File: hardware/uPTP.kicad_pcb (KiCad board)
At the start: 4 copper layers, 40 x 50 mm, 78 parts, among them J1 PPS_UFL, J2 PPS_SMA, J3 LED, J4 UART_HDR, J5 HC-RJ45-055-7, J6 AUX_PWR, J7 PROG, U1 XC6206P332MR-G, U2 SI3404-A-GMR, U3 CH32V307WCU6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

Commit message: Route one
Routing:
- net /Ethernet and POE/ETH_D_ISO_RX_P: track 6.89 -> 9.89 mm
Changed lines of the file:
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@@
+	)
+	(segment
+		(start 160.53 111.13)
+		(end 159.7 110.3)
+		(width 0.3)
+		(layer "F.Cu")
+		(net 14)
 	)
 	(segment
 		(start 160.53 113.4425)
-		(end 160.53 112)
+		(end 160.53 111.13)
 		(width 0.3)
 		(layer "F.Cu")
@@
 	)
 	(segment
-		(start 160.53 112)
-		(end 159.275 110.745)
+		(start 159.7 110.3)
+		(end 159.7 106.7)
 		(width 0.3)
 		(layer "F.Cu")
@@
 	)
 	(segment
-		(start 159.275 110.745)
-		(end 159.275 106.275)
+		(start 159.7 106.7)
+		(end 158.885 105.885)
 		(width 0.3)
 		(layer "F.Cu")
@@
 	)
 	(segment
-		(start 159.275 106.275)
-		(end 158.885 105.885)
-		(width 0.3)
-		(layer "F.Cu")
-		(net 14)
+		(start 157.942794 109.73087)
+		(end 158.636258 110.424334)
+		(width 0.3)
+		(layer "F.Cu")
+		(net 15)
 	)
 	(segment
 		(start 157.47 113.4425)
-		(end 157.47 112)
-		(width 0.3)
-		(layer "F.Cu")
-		(net 15)
-	)
-	(segment
-		(start 158.425 108.425)
+		(end 157.47 111.93)
+		(width 0.3)
+		(layer "F.Cu")
+		(net 15)
+	)
+	(segment
+		(start 158.97567 110.424333)
+		(end 159.060522 110.339479)
+		(width 0.3)
+		(layer "F.Cu")
+		(net 15)
+	)
+	(segment
+		(start 158.725 108.425)
 		(end 157.2 108.425)
 		(width 0.3)
@@
 	)
 	(segment
-		(start 157.47 112)
-		(end 158.725 110.745)
-		(width 0.3)
-		(layer "F.Cu")
-		(net 15)
-	)
-	(segment
-		(start 158.725 110.745)
-		(end 158.725 108.725)
-		(width 0.3)
-		(layer "F.Cu")
-		(net 15)
-	)
-	(segment
-		(start 158.725 108.725)
-		(end 158.425 108.425)
+		(start 159.060522 110.339479)
+		(end 159.15 110.25)
+		(width 0.3)
+		(layer "F.Cu")
+		(net 15)
+	)
+	(segment
+		(start 159.15 108.85)
+		(end 158.725 108.425)
+		(width 0.3)
+		(layer "F.Cu")
+		(net 15)
+	)
+	(segment
+		(start 159.15 110.25)
+		(end 159.15 108.85)
+		(width 0.3)
+		(layer "F.Cu")
+		(net 15)
+	)
+	(segment
+		(start 158.211993 110.848596)
+		(end 157.51853 110.155133)
+		(width 0.3)
+		(layer "F.Cu")
+		(net 15)
+	)
+	(segment
+		(start 157.47 111.93)
+		(end 158.211992 111.188008)
+		(width 0.3)
+		(layer "F.Cu")
+		(net 15)
+	)
+	(segment
+		(start 157.518529 109.815723)
+		(end 157.603384 109.730869)
+		(width 0.3)
+		(layer "F.Cu")
+		(net 15)
+	)
+	(arc
+		(start 157.603384 109.730869)
+		(mid 157.773089 109.660575)
+		(end 157.942794 109.73087)
+		(width 0.3)
+		(layer "F.Cu")
+		(net 15)
+	)
+	(arc
+		(start 158.211992 111.188008)
+		(mid 158.282287 111.018302)
+		(end 158.211993 110.848596)
+		(width 0.3)
+		(layer "F.Cu")
+		(net 15)
+	)
+	(arc
+		(start 158.636258 110.424334)
+		(mid 158.805963 110.494629)
+		(end 158.97567 110.424333)
+		(width 0.3)
+		(layer "F.Cu")
+		(net 15)
+	)
+	(arc
+		(start 157.51853 110.155133)
+		(mid 157.448236 109.985427)
+		(end 157.518529 109.815723)
 		(width 0.3)
 		(layer "F.Cu")
@@
 		)
 	)
+	(generated
+		(type tuning_pattern)
+		(name "Tuning Pattern")
+		(layer "F.Cu")
+		(base_line
+			(pts
+				(xy 158.211992 111.188008) (xy 159.15 110.25) (xy 159.15 108.85) (xy 158.725 108.425) (xy 157.2 108.425)
+			)
+		)
+		(base_line_coupled
+			(pts
+				(xy 159.7 110.3) (xy 159.7 108.425)
+			)
+		)
+		(corner_radius_percent 80)
+		(end
+			(xy 157.2 108.425)
+		)
+		(initial_side "left")
+		(last_diff_pair_gap 0.18)
+		(last_netname "/Ethernet and POE/ETH_D_ISO_RX_P")
+		(last_status "too_short")
+		(last_track_width 0.3)
+		(last_tuning "-0.0000 mm (too short)")
+		(max_amplitude 1.5)
+		(min_amplitude 0.2)
+		(min_spacing 0.6)
+		(origin
+			(xy 158.211992 111.188008)
+		)
+		(override_custom_rules no)
+		(rounded yes)
+		(single_sided no)
+		(target_length 1000000)
+		(target_length_max 1000000)
+		(target_length_min 0)
+		(target_skew 0)
+		(target_skew_max 2147.483647)
+		(target_skew_min 0)
+		(tuning_mode "diff_pair_skew")
+		(members "0bae2fc2-0211-45f2-b836-eb4cafed9c5f" "277517a9-859e-45f5-9af7-aa420a2b5a6d"
+			"5b8daaf6-95e9-43ba-83e5-7fa846d3aed7" "5c5d8d0c-bf78-4b6e-a43a-62fd2599fa16"
+			"5cfc8858-2205-4a4b-a7d7-186fc4d642b2" "72fc6440-39a9-4567-8914-2f6c557ffe45"
+			"79a215ad-b56f-4a34-89d0-93d5ca94d08a" "8e7def69-ecf8-4a06-9879-d4727dc86b5c"
+			"95469f03-8aef-4034-a113-e60f53eb121f" "d9926ceb-a356-417e-8caa-e14e1cfa22e8"
+			"e493b56a-8677-492b-b57a-b9f674e9be6f" "fd0d77c2-6f58-4c50-8de8-89af1b98e4d6"
+		)
+	)

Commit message: All length match
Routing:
- net /Ethernet and POE/ETH_D_ISO_TX_P: track 13.2 -> 21.8 mm
- net /Ethernet and POE/ETH_D_TX_P: track 12.1 -> 13.2 mm
- net /Ethernet and POE/ETH_D_ISO_TX_N: track 21.3 -> 21.9 mm

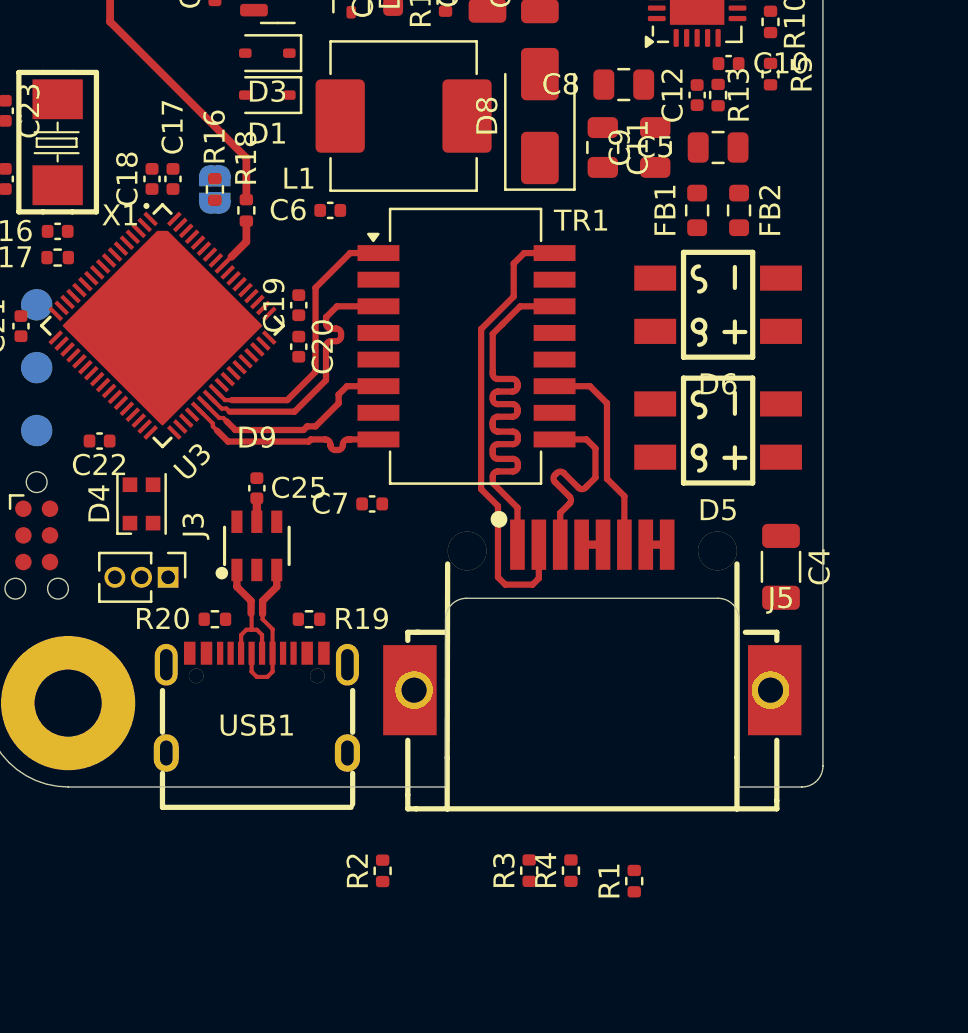
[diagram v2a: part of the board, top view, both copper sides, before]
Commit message: ISO ETH Section Done
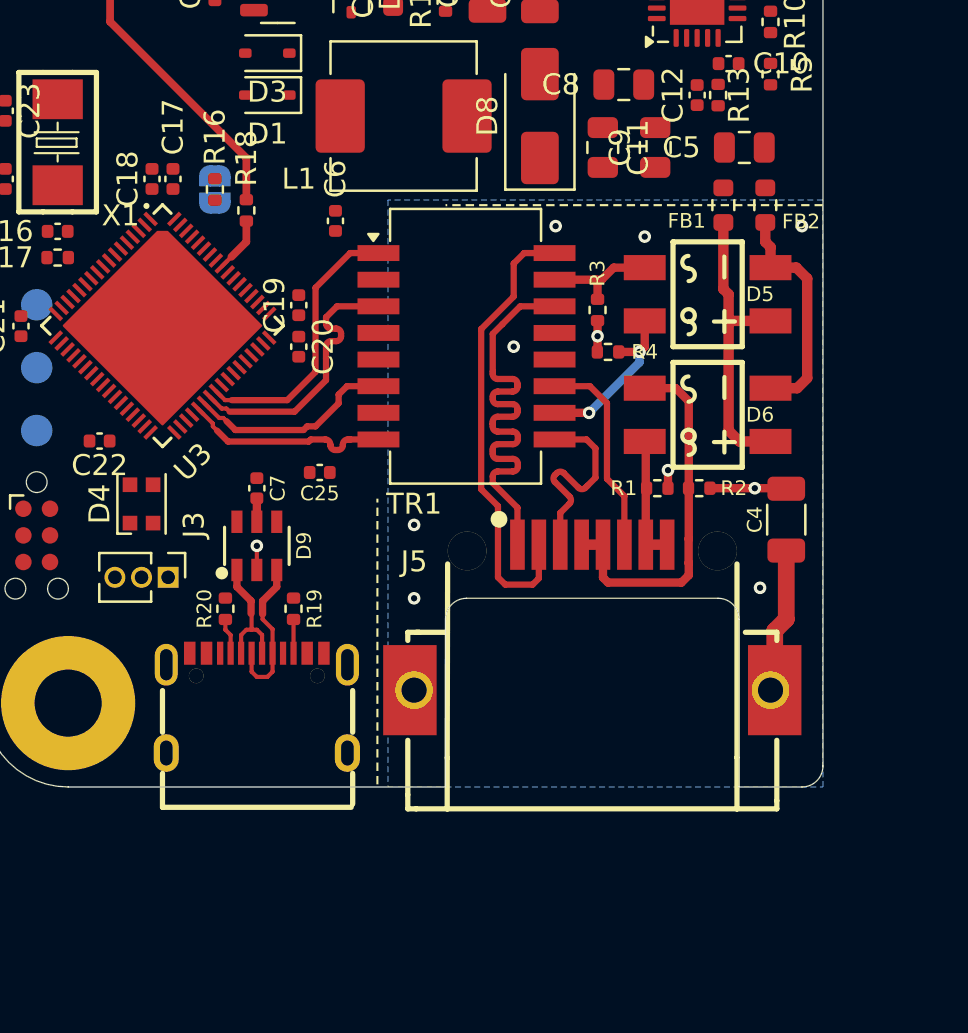
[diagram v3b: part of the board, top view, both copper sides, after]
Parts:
- moved R3 26.9 mm to (159.2, 102.2), turned to -90 degrees
- moved R4 24.8 mm to (159.8, 104.2), turned to 180 degrees
- moved R2 23.7 mm to (164.1, 110.8), turned to 0 degrees
- moved R1 18.8 mm to (162.1, 110.8), turned to 0 degrees
- moved D5 6.52 mm to (164.5, 101.5)
- moved D6 5.27 mm to (164.5, 107.2)
- moved C7 2.92 mm to (146.0, 110.0)
- moved C4 2.26 mm to (168.2, 112.2)
- moved FB1 1.27 mm to (165.2, 97.2)
- moved FB2 1.27 mm to (167.2, 97.2)
- moved C5 1.25 mm to (166.2, 94.5)
- moved R19 0.89 mm to (144.8, 116.5), turned to 90 degrees
- moved R20 0.71 mm to (141.5, 116.5), turned to 90 degrees
- moved C6 0.56 mm to (146.8, 98.0), turned to 90 degrees
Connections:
- net Net-(C11-Pad2) renamed /Ethernet and POE/ETH_C_MID
- D5 pad 2: /Ethernet and POE/ETH_TX1 -> /Ethernet and POE/ETH_RX1
- D5 pad 4: /Ethernet and POE/ETH_TX2 -> /Ethernet and POE/ETH_TX1
- D6 pad 4: /Ethernet and POE/ETH_RX1 -> /Ethernet and POE/ETH_TX2
- H1 pad 1: unconnected-(H1-Pad1) -> GND
- H2 pad 1: unconnected-(H2-Pad1) -> GND
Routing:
- net /Ethernet and POE/ETH_TX2: track 1.02 -> 17.6 mm
- net /Ethernet and POE/ETH_POE_P: track 0.00 -> 14.2 mm
- net /Ethernet and POE/ETH_POE_N: track 0.00 -> 10.9 mm
- net /Ethernet and POE/ETH_RX1: track 0.00 -> 8.12 mm, vias 0 -> 2
- net SHIELD: track 0.00 -> 6.89 mm, vias 0 -> 7
- net /Ethernet and POE/ETH_BOB_SMITH: track 0.00 -> 6.00 mm, vias 0 -> 3
- net /Ethernet and POE/ETH_TX1: track 0.00 -> 5.50 mm
- net /Ethernet and POE/ETH_RX2: track 1.02 -> 5.96 mm
- net /USB/USB_CC1: track 0.00 -> 1.46 mm
- net /USB/USB_CC2: track 0.00 -> 1.36 mm
- net GND: track 0.00 -> 1.15 mm, vias 0 -> 1
- added copper zone on In2.Cu, net /Ethernet and POE/ETH_BOB_SMITH
- added copper zone on In1.Cu, net GND
- added copper zone on B.Cu, net SHIELD
- added copper zone on In1.Cu, net SHIELD

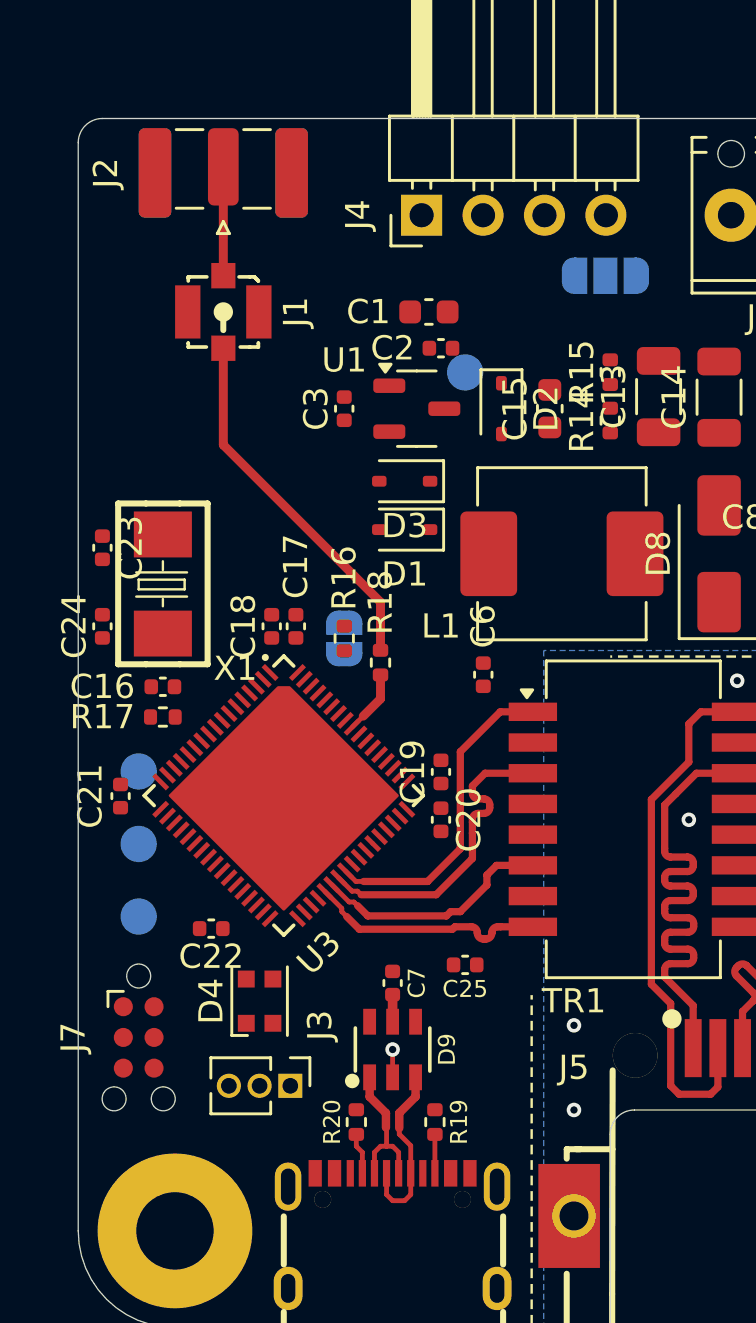
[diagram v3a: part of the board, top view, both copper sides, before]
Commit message: All footprints 3D plus some more routing
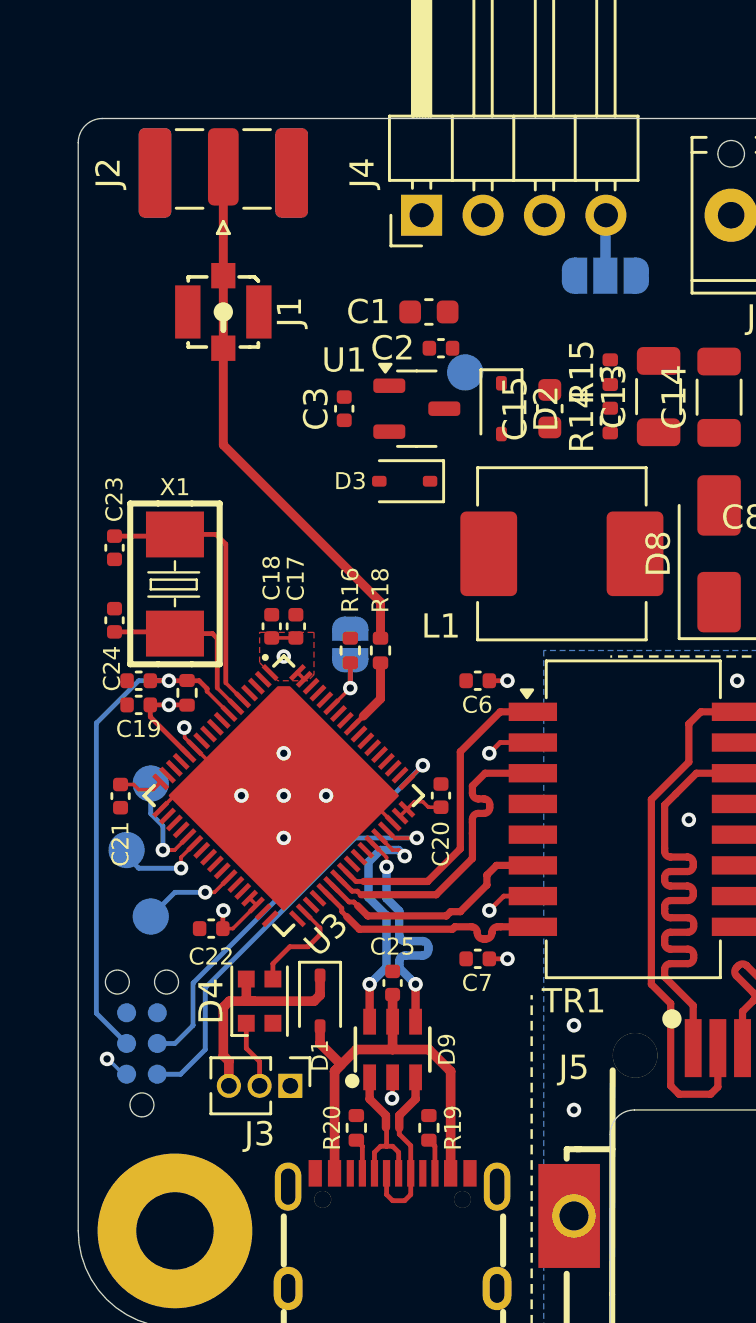
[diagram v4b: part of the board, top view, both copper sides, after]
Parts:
- J7: moved to B.Cu
- moved D1 19.8 mm to (140.0, 111.5), turned to -90 degrees
- moved C19 12.8 mm to (132.5, 99.2), turned to 180 degrees
- moved R17 1.41 mm to (134.5, 98.8), turned to 90 degrees
- moved C16 1.03 mm to (132.5, 98.2)
- moved C20 1.00 mm to (145.0, 103.0), turned to 90 degrees
- moved TP3 0.71 mm to (133.0, 102.5)
- moved C7 0.58 mm to (146.5, 109.8)
- moved C24 0.56 mm to (131.5, 95.8)
- moved R16 0.56 mm to (141.2, 97.0)
- moved TP4 0.56 mm to (132.0, 105.2)
- moved C23 0.50 mm to (131.5, 92.8)
- moved R18 0.50 mm to (142.5, 97.0)
- moved TP2 0.50 mm to (133.0, 108.0)
- moved X1 0.50 mm to (134.0, 94.2)
- moved JP2 0.35 mm to (141.2, 96.8)
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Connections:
- U3 pad 44: /MCU/NMEA_UART_TX -> unconnected-(U3-PA9-Pad44)
- U3 pad 45: /MCU/NMEA_UART_RX -> unconnected-(U3-PA10-Pad45)
- U3 pad 54: unconnected-(U3-PC10-Pad54) -> /MCU/NMEA_UART_TX
- U3 pad 55: unconnected-(U3-PC11-Pad55) -> /MCU/NMEA_UART_RX
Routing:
- net /MCU/~{RST}: track 0.00 -> 21.1 mm, vias 0 -> 1
- net +3V3: track 0.00 -> 19.0 mm, vias 0 -> 8
- net /MCU/SWCLK: track 0.00 -> 17.9 mm, vias 0 -> 1
- net /MCU/SWDIO: track 0.00 -> 17.7 mm, vias 0 -> 1
- net +5V_USB: track 1.12 -> 18.6 mm
- net GND: track 1.15 -> 15.0 mm, vias 1 -> 7
- net /MCU/XTAL_IN: track 0.00 -> 11.5 mm
- net /MCU/USB_D_N: track 0.00 -> 10.5 mm, vias 0 -> 2
- net /MCU/USB_D_P: track 0.00 -> 10.2 mm, vias 0 -> 2
- net +5V: track 0.00 -> 9.57 mm
- net /MCU/XTAL_OUT: track 0.00 -> 7.50 mm
- net /MCU/DEBUG_1: track 0.00 -> 4.46 mm, vias 0 -> 1
- net /LED_STAGE_1: track 0.00 -> 4.29 mm
- net /MCU/DEBUG_2: track 0.00 -> 3.96 mm, vias 0 -> 1
- net /MCU/MCU_BOOT1: track 0.00 -> 3.90 mm, vias 0 -> 1
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- added copper zone on F.Cu, net +3V3
- added copper zone on In2.Cu, net +3V3
- added copper zone on In2.Cu, net GND

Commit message: Fix aux pwr oops
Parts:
- added TP5: SWO, TestPoint:TestPoint_Pad_D1.5mm, F.Cu at (159.8, 89.0)
- moved D7 24.8 mm to (151.2, 82.8)
- moved C13 0.50 mm to (154.0, 87.0)
- moved C14 0.50 mm to (156.5, 87.0)
- moved R14 0.50 mm to (152.0, 88.0)
- moved R15 0.50 mm to (152.0, 86.0)
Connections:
- J6 pad 1: /Ethernet and POE/ETH_EROUT_RC -> /Ethernet and POE/ETH_POE_FILT_N
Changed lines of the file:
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@@
 	(footprint "Resistor_SMD:R_0402_1005Metric"
 		(layer "F.Cu")
-		(at 152 85.49 90)
+		(at 152 85.99 90)
 		(descr "Resistor SMD 0402 (1005 Metric), square (rectangular) end terminal, IPC-7351 nominal, (Body size source: IPC-SM-782 page 72, https://www.pcb-3d.com/wordpress/wp-content/uploads/ipc-sm-782a_amendment_1_and_2.pdf), generated with kicad-footprint-generator")
 		(tags "resistor")
@@
 	(footprint "Diode_SMD:D_SMA"
 		(layer "F.Cu")
-		(at 175 75.5)
+		(at 151.25 82.75)
 		(descr "Diode SMA (DO-214AC)")
 		(tags "Diode SMA (DO-214AC)")
@@
 			)
 		)
+		(property "LCSC Part" "C965555"
+			(at 0 0 90)
+			(unlocked yes)
+			(layer "F.Fab")
+			(hide yes)
+			(effects
+				(font
+					(size 1 1)
+					(thickness 0.15)
+				)
+			)
+		)
 		(property ki_fp_filters "LED*WS2812*-2020_PLCC4*")
 		(sheetname "/")
@@
 	(footprint "Capacitor_SMD:C_1206_3216Metric"
 		(layer "F.Cu")
-		(at 156.5 86.525 90)
+		(at 156.5 87.025 90)
 		(descr "Capacitor SMD 1206 (3216 Metric), square (rectangular) end terminal, IPC-7351 nominal, (Body size source: IPC-SM-782 page 76, https://www.pcb-3d.com/wordpress/wp-content/uploads/ipc-sm-782a_amendment_1_and_2.pdf), generated with kicad-footprint-generator")
 		(tags "capacitor")
@@
 	(footprint "Capacitor_SMD:C_1206_3216Metric"
 		(layer "F.Cu")
-		(at 154 86.5 90)
+		(at 154 87 90)
 		(descr "Capacitor SMD 1206 (3216 Metric), square (rectangular) end terminal, IPC-7351 nominal, (Body size source: IPC-SM-782 page 76, https://www.pcb-3d.com/wordpress/wp-content/uploads/ipc-sm-782a_amendment_1_and_2.pdf), generated with kicad-footprint-generator")
 		(tags "capacitor")
@@
 			(remove_unused_layers no)
 			(roundrect_rratio 0.113636)
-			(net 65 "/Ethernet and POE/ETH_EROUT_RC")
+			(net 69 "/Ethernet and POE/ETH_POE_FILT_N")
 			(pinfunction "Pin_1")
 			(pintype "passive")
@@
 		)
 	)
+	(footprint "TestPoint:TestPoint_Pad_D1.5mm"
+		(layer "F.Cu")
+		(at 159.75 89)
+		(descr "SMD pad as test Point, diameter 1.5mm")
+		(tags "test point SMD pad")
+		(property "Reference" "TP5"
+			(at 0 -1.648 0)
+			(layer "F.SilkS")
+			(effects
+				(font
+					(size 1 1)
+					(thickness 0.15)
+				)
+			)
+		)
+		(property "Value" "SWO"
+			(at 0 1.75 0)
+			(layer "F.Fab")
+			(effects
+				(font
+					(size 1 1)
+					(thickness 0.15)
+				)
+			)
+		)
+		(property "Datasheet" ""
+			(at 0 0 0)
+			(unlocked yes)
+			(layer "F.Fab")
+			(hide yes)
+			(effects
+				(font
+					(size 1.27 1.27)
+					(thickness 0.15)
+				)
+			)
+		)
+		(property "Description" "test point"
+			(at 0 0 0)
+			(unlocked yes)
+			(layer "F.Fab")
+			(hide yes)
+			(effects
+				(font
+					(size 1.27 1.27)
+					(thickness 0.15)
+				)
+			)
+		)
+		(property ki_fp_filters "Pin* Test*")
+		(sheetname "/Ethernet and POE/")
+		(sheetfile "ethernet.kicad_sch")
+		(attr exclude_from_pos_files)
+		(fp_circle
+			(center 0 0)
+			(end 0 0.95)
+			(stroke
+				(width 0.12)
+				(type solid)
+			)
+			(fill no)
+			(layer "F.SilkS")
+		)
+		(fp_circle
+			(center 0 0)
+			(end 1.25 0)
+			(stroke
+				(width 0.05)
+				(type solid)
+			)
+			(fill no)
+			(layer "F.CrtYd")
+		)
+		(fp_text user "${REFERENCE}"
+			(at 0 -1.65 0)
+			(layer "F.Fab")
+			(effects
+				(font
+					(size 1 1)
+					(thickness 0.15)
+				)
+			)
+		)
+		(pad "1" smd circle
+			(at 0 0)
+			(size 1.5 1.5)
+			(layers "F.Cu" "F.Mask")
+			(net 67 "/Ethernet and POE/ETH_BUCK_SW")
+			(pinfunction "1")
+			(pintype "passive")
+		)
+		(embedded_fonts no)
+	)
 	(footprint "Inductor_SMD:L_Changjiang_FXL0630"
 		(layer "F.Cu")
@@
 	(footprint "Resistor_SMD:R_0402_1005Metric"
 		(layer "F.Cu")
-		(at 152 87.49 90)
+		(at 152 87.99 90)
 		(descr "Resistor SMD 0402 (1005 Metric), square (rectangular) end terminal, IPC-7351 nominal, (Body size source: IPC-SM-782 page 72, https://www.pcb-3d.com/wordpress/wp-content/uploads/ipc-sm-782a_amendment_1_and_2.pdf), generated with kicad-footprint-generator")
 		(tags "resistor")

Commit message: Backup before relayout
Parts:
- moved TP5 1.75 mm to (159.8, 87.2)
- moved JP1 0.50 mm to (151.8, 82.0)
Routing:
- net /UART_PWR: track 2.51 -> 3.01 mm
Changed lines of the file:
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@@
 	(footprint "TestPoint:TestPoint_Pad_D1.5mm"
 		(layer "F.Cu")
-		(at 159.75 89)
+		(at 159.75 87.25)
 		(descr "SMD pad as test Point, diameter 1.5mm")
 		(tags "test point SMD pad")
@@
 	(footprint "Jumper:SolderJumper-3_P1.3mm_Open_RoundedPad1.0x1.5mm_NumberLabels"
 		(layer "B.Cu")
-		(at 151.8 81.5)
+		(at 151.8 82)
 		(descr "SMD Solder 3-pad Jumper, 1x1.5mm rounded Pads, 0.3mm gap, open, labeled with numbers")
 		(tags "solder jumper open")
@@
 	)
 	(segment
-		(start 151.8 81.5)
+		(start 151.8 82)
 		(end 151.8 79.02)
 		(width 0.43)
@@
 			)
 		)
+	)
+	(zone
+		(net 0)
+		(net_name "")
+		(layer "In1.Cu")
+		(name "BUCK_ISO_GND")
+		(hatch edge 0.5)
+		(connect_pads
+			(clearance 0)
+		)
+		(min_thickness 0.25)
+		(filled_areas_thickness no)
+		(keepout
+			(tracks allowed)
+			(vias allowed)
+			(pads allowed)
+			(copperpour not_allowed)
+			(footprints allowed)
+		)
+		(placement
+			(enabled no)
+			(sheetname "/")
+		)
+		(fill
+			(thermal_gap 0.2)
+			(thermal_bridge_width 0.5)
+		)
+		(polygon
+			(pts
+				(xy 170 75) (xy 155 75) (xy 155 97.25) (xy 170 97.25)
+			)
+		)
